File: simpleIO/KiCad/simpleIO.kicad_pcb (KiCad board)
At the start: 2 copper layers, 42.2 x 47.1 mm, 48 parts, among them J1 Conn_02x17_Odd_Even

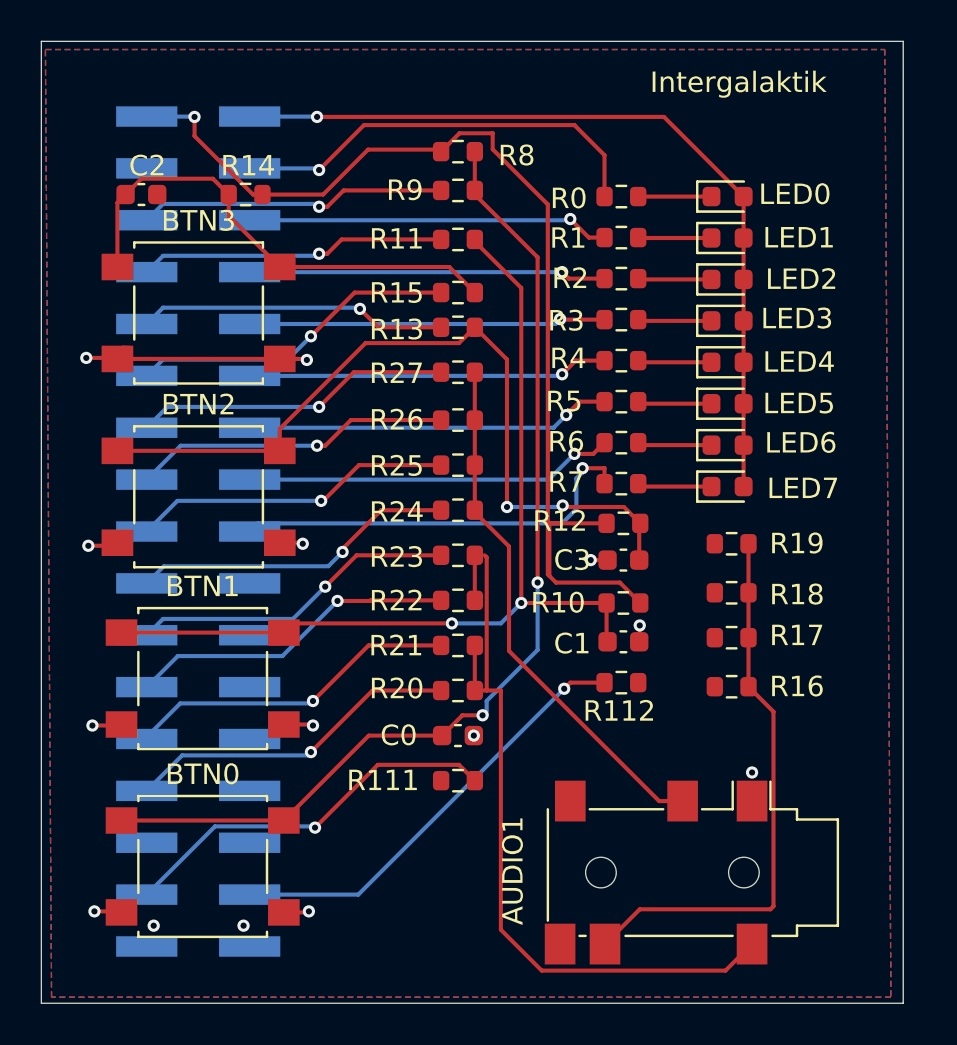
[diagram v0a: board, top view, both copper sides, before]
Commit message: Cleanup - switch to 4layer
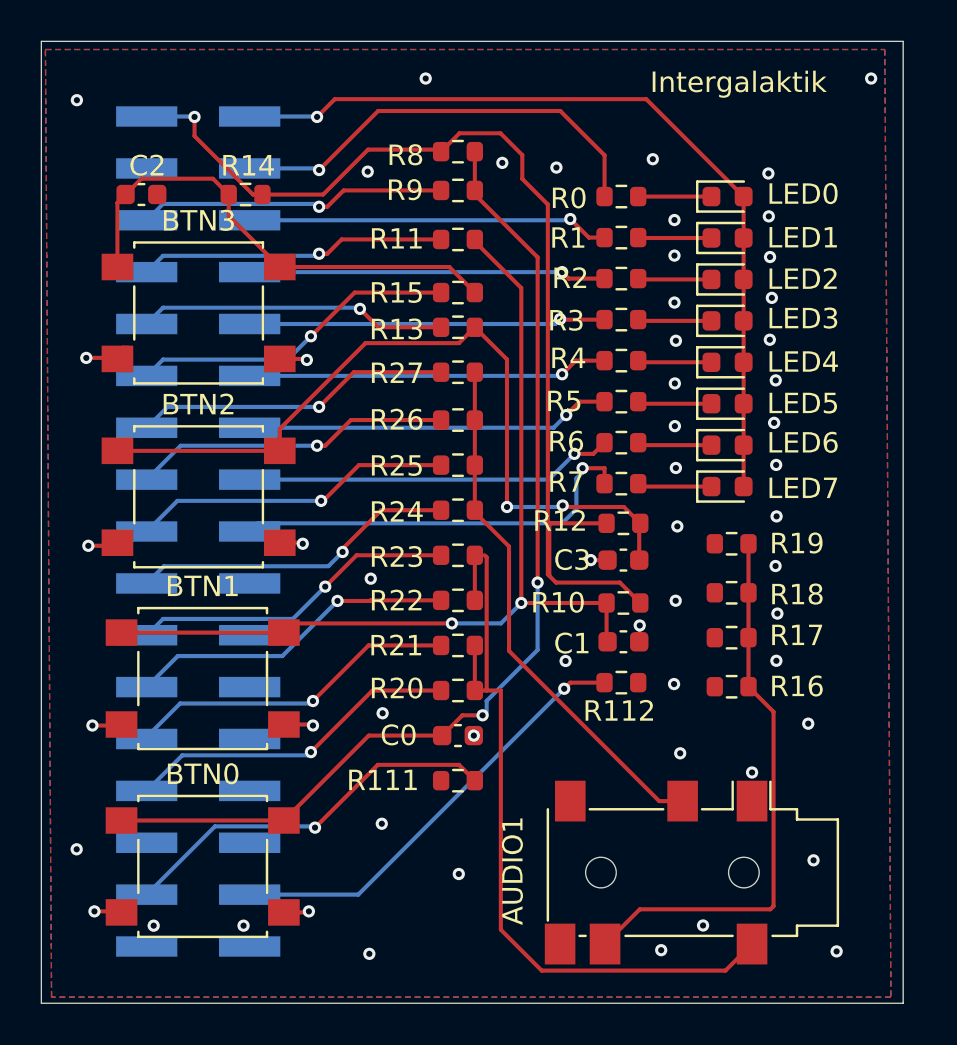
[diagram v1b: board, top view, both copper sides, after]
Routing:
- net GND: track 22.0 -> 14.1 mm, vias 14 -> 56
- net +1V8: track 40.0 -> 40.8 mm
- net /WC_B3: track 21.2 -> 21.8 mm
- added copper zone on In1.Cu, net GND
- added copper zone on In2.Cu, net GND
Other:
- copper layers 2 -> 4

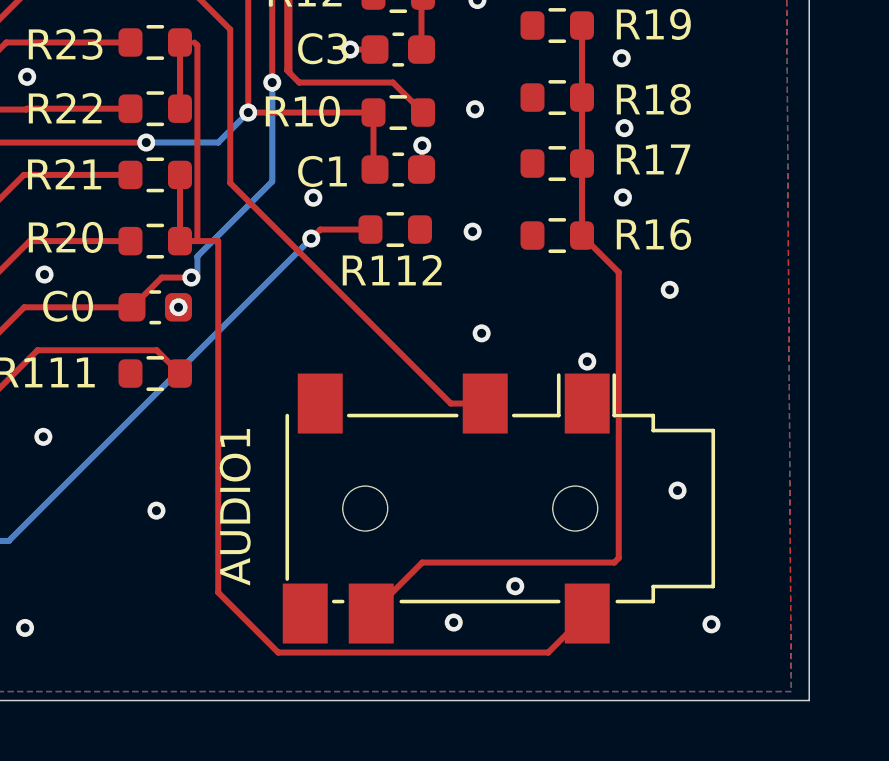
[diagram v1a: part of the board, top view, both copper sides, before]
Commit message: Changing audio connector
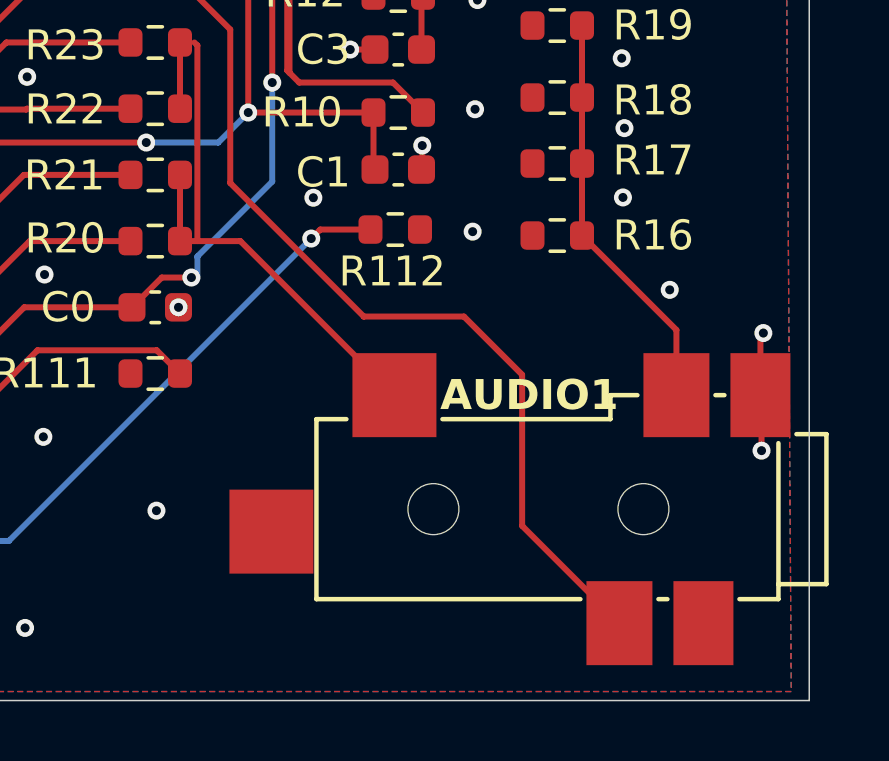
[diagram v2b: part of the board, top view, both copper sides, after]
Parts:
- AUDIO1: footprint Connector_Audio:Jack_3.5mm_PJ311_Horizontal -> audio-jack:CUI_SJ-43516-SMT
- moved AUDIO1 3.57 mm to (140.8, 93.3)
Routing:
- net /AUDIO_L: track 37.6 -> 20.3 mm
- net /AUDIO_V: track 27.3 -> 13.6 mm
- net /AUDIO_R: track 25.9 -> 36.4 mm
- net GND: track 14.1 -> 18.1 mm, vias 56 -> 52

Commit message: Update
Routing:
- net /AUDIO_L: track 20.3 -> 15.9 mm
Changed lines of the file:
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@@
+	)
+	(segment
+		(start 128.325 79.97142)
+		(end 128.325 77.764278)
+		(width 0.2)
+		(layer "F.Cu")
+		(net 3)
+	)
+	(segment
+		(start 128.325 79.97142)
+		(end 128.325 84.385704)
+		(width 0.2)
+		(layer "F.Cu")
+		(net 3)
+	)
+	(segment
+		(start 128.325 84.385704)
+		(end 130.338204 84.385704)
+		(width 0.2)
+		(layer "F.Cu")
+		(net 3)
 	)
 	(segment
@@
 	)
 	(segment
-		(start 130.338204 84.385704)
-		(end 128.425 84.385704)
-		(width 0.2)
-		(layer "F.Cu")
-		(net 3)
-	)
-	(segment
-		(start 128.325 79.97142)
-		(end 128.325 77.764278)
-		(width 0.2)
-		(layer "F.Cu")
-		(net 3)
-	)
-	(segment
-		(start 128.904999 84.385704)
-		(end 128.904999 77.864278)
-		(width 0.2)
-		(layer "F.Cu")
-		(net 3)
-	)
-	(segment
-		(start 128.325 82.178562)
-		(end 128.325 84.385704)
-		(width 0.2)
-		(layer "F.Cu")
-		(net 3)
-	)
-	(segment
-		(start 128.904999 77.864278)
-		(end 128.804999 77.764278)
-		(width 0.2)
-		(layer "F.Cu")
-		(net 3)
-	)
-	(segment
 		(start 109.3 68.1)
 		(end 110.775 68.1)
@@
 	)
 	(segment
-		(start 137.79 86.9)
-		(end 139.73 88.84)
-		(width 0.2)
-		(layer "F.Cu")
-		(net 6)
-	)
-	(segment
-		(start 134.45 86.898529)
-		(end 134.45 86.9)
+		(start 133.77 86.9)
+		(end 136.61 86.9)
+		(width 0.2)
+		(layer "F.Cu")
+		(net 6)
+	)
+	(segment
+		(start 129.41 76.742136)
+		(end 129.41 82.54)
+		(width 0.2)
+		(layer "F.Cu")
+		(net 6)
+	)
+	(segment
+		(start 139.73 93.8775)
+		(end 142.9725 97.12)
+		(width 0.2)
+		(layer "F.Cu")
+		(net 6)
+	)
+	(segment
+		(start 129.41 82.54)
+		(end 133.77 86.9)
+		(width 0.2)
+		(layer "F.Cu")
+		(net 6)
+	)
+	(segment
+		(start 139.73 90.02)
+		(end 139.73 93.8775)
 		(width 0.2)
 		(layer "F.Cu")
@@
 	)
 	(segment
-		(start 139.73 93.8775)
-		(end 142.9725 97.12)
-		(width 0.2)
-		(layer "F.Cu")
-		(net 6)
-	)
-	(segment
-		(start 130 82.448529)
-		(end 134.45 86.898529)
-		(width 0.2)
-		(layer "F.Cu")
-		(net 6)
-	)
-	(segment
-		(start 134.45 86.9)
-		(end 137.79 86.9)
-		(width 0.2)
-		(layer "F.Cu")
-		(net 6)
-	)
-	(segment
-		(start 139.73 88.84)
-		(end 139.73 93.8775)
+		(start 136.61 86.9)
+		(end 139.73 90.02)
 		(width 0.2)
 		(layer "F.Cu")
@@
 	)
 	(segment
-		(start 130 77.332136)
-		(end 130 82.448529)
-		(width 0.2)
-		(layer "F.Cu")
-		(net 6)
-	)
-	(segment
 		(start 128.225 75.557136)
-		(end 130 77.332136)
-		(width 0.2)
-		(layer "F.Cu")
+		(end 129.41 76.742136)
+		(width 0.2)
+		(layer "F.Cu")
